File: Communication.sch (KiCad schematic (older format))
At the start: 8 parts

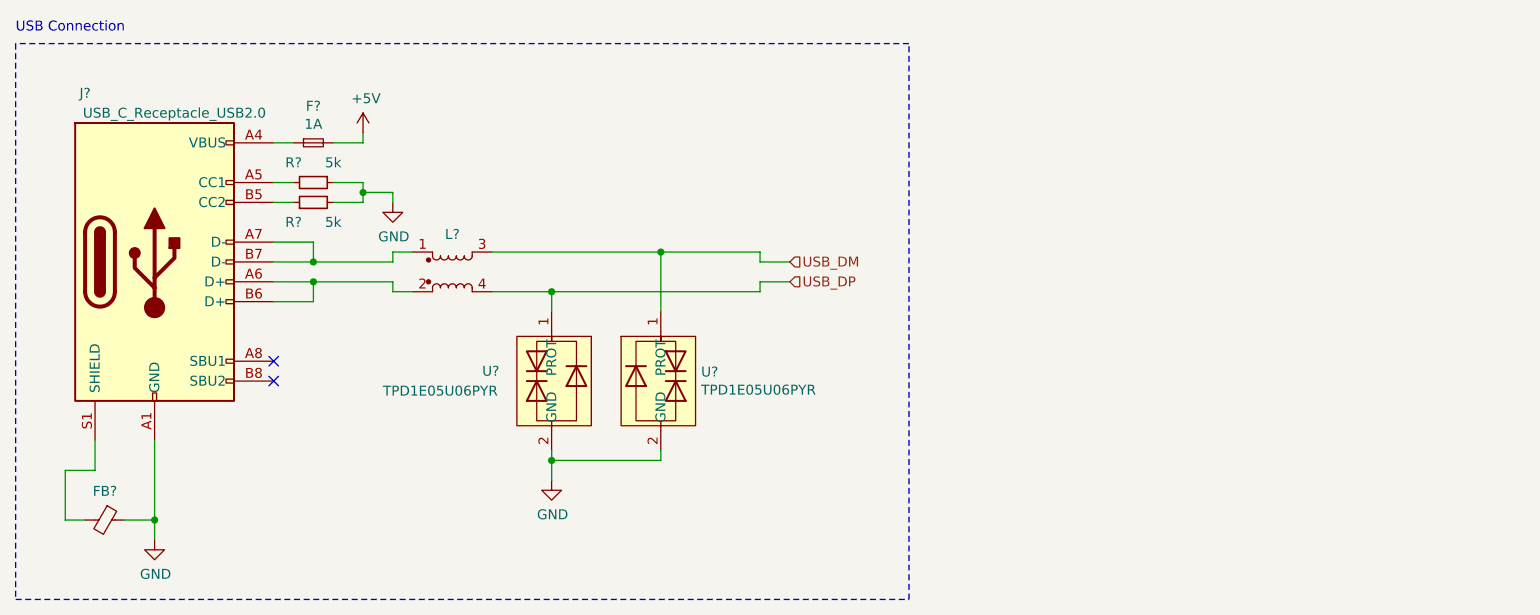
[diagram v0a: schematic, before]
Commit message: Added display driver for 7 segment
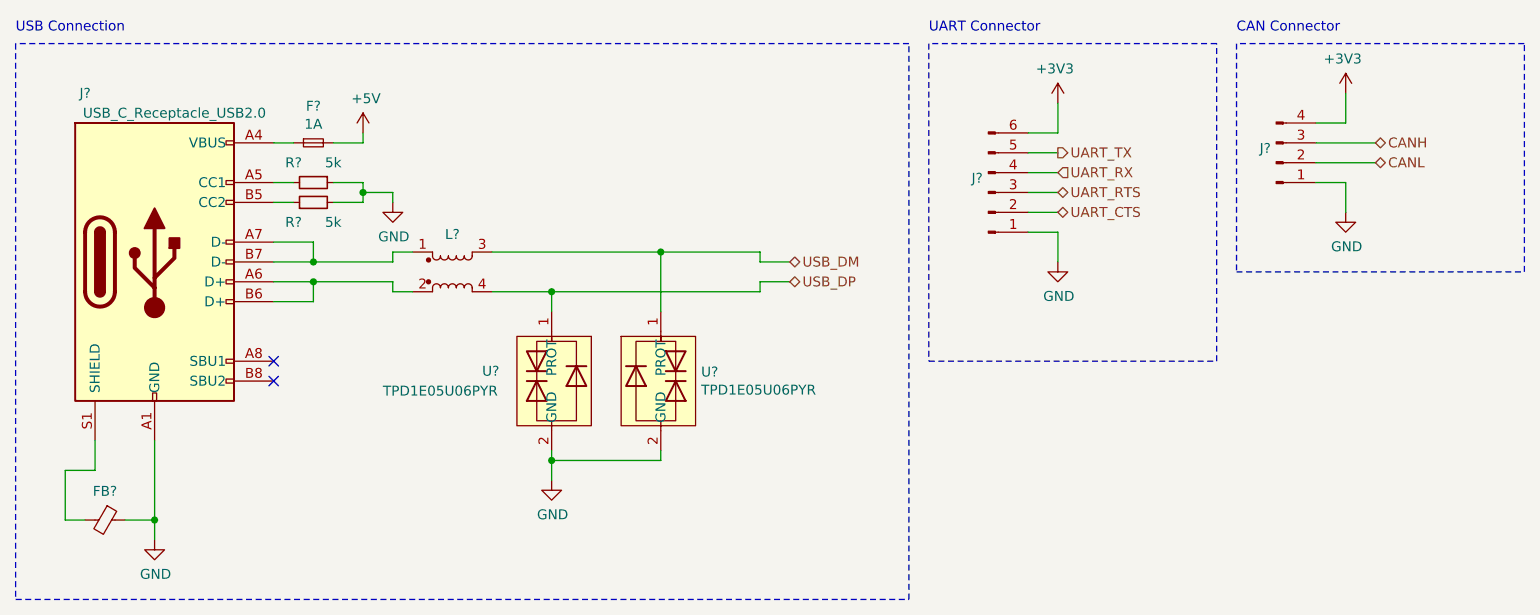
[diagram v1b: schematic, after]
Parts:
- added J?: Conn_01x06_Male, symbol Connector:Conn_01x06_Male
- added J?: Conn_01x04_Male, symbol Connector:Conn_01x04_Male
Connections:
- net GND: now also J?.1 (Pin_1), J?.1 (Pin_1)
- new net +3V3: J?.4 (Pin_4), J?.6 (Pin_6)
- new net CANH: J?.3 (Pin_3)
- new net CANL: J?.2 (Pin_2)
- new net UART_CTS: J?.2 (Pin_2)
- new net UART_RTS: J?.3 (Pin_3)
- new net UART_RX: J?.4 (Pin_4)
- new net UART_TX: J?.5 (Pin_5)
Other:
- note added: "CAN Connector"
- note added: "UART Connector"
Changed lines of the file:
@@
 $Descr A4 11693 8268
 encoding utf-8
-Sheet 1 7
+Sheet 5 7
 Title ""
 Date ""
@@
 Wire Wire Line
 	1850 1850 2050 1850
-Text HLabel 4450 1850 2    50   Input ~ 0
+Text HLabel 4450 1850 2    50   BiDi ~ 0
 USB_DP
 Wire Wire Line
@@
 	1    0    0    -1
 $EndComp
-Text HLabel 4450 1750 2    50   Input ~ 0
+Text HLabel 4450 1750 2    50   BiDi ~ 0
 USB_DM
 NoConn ~ 1850 2350
@@
 Text Notes 550  600  0    50   ~ 0
 USB Connection
+Text HLabel 5800 1200 2    50   Output ~ 0
+UART_TX
+Text HLabel 5800 1300 2    50   Input ~ 0
+UART_RX
+Text HLabel 5800 1400 2    50   BiDi ~ 0
+UART_RTS
+Text HLabel 5800 1500 2    50   BiDi ~ 0
+UART_CTS
+$Comp
+L Connector:Conn_01x06_Male J?
+U 1 1 5F695AB7
+P 5450 1400
+F 0 "J?" H 5422 1328 50  0000 R CNN
+F 1 "Conn_01x06_Male" H 5422 1373 50  0001 R CNN
+F 2 "" H 5450 1400 50  0001 C CNN
+F 3 "~" H 5450 1400 50  0001 C CNN
+	1    5450 1400
+	1    0    0    1
+$EndComp
+Wire Wire Line
+	5800 1200 5650 1200
+Wire Wire Line
+	5800 1300 5650 1300
+Wire Wire Line
+	5800 1400 5650 1400
+Wire Wire Line
+	5800 1500 5650 1500
+$Comp
+L power:GND #PWR?
+U 1 1 5F699450
+P 7250 1500
+F 0 "#PWR?" H 7250 1250 50  0001 C CNN
+F 1 "GND" H 7255 1327 50  0000 C CNN
+F 2 "" H 7250 1500 50  0001 C CNN
+F 3 "" H 7250 1500 50  0001 C CNN
+	1    7250 1500
+	1    0    0    -1
+$EndComp
+Wire Wire Line
+	5800 1600 5650 1600
+Wire Wire Line
+	5800 1600 5800 1750
+Wire Wire Line
+	5650 1100 5800 1100
+Wire Wire Line
+	5800 1100 5800 950
+$Comp
+L power:+3V3 #PWR?
+U 1 1 5F69C601
+P 5800 950
+F 0 "#PWR?" H 5800 800 50  0001 C CNN
+F 1 "+3V3" H 5815 1123 50  0000 C CNN
+F 2 "" H 5800 950 50  0001 C CNN
+F 3 "" H 5800 950 50  0001 C CNN
+	1    5800 950
+	-1   0    0    -1
+$EndComp
+Wire Notes Line
+	5150 650  5150 2250
+Wire Notes Line
+	5150 2250 6600 2250
+Wire Notes Line
+	6600 2250 6600 650
+Wire Notes Line
+	6600 650  5150 650
+Text Notes 5150 600  0    50   ~ 0
+UART Connector
+$Comp
+L Connector:Conn_01x04_Male J?
+U 1 1 5F6AA35C
+P 6900 1250
+F 0 "J?" H 6873 1178 50  0000 R CNN
+F 1 "Conn_01x04_Male" H 6872 1223 50  0001 R CNN
+F 2 "" H 6900 1250 50  0001 C CNN
+F 3 "~" H 6900 1250 50  0001 C CNN
+	1    6900 1250
+	1    0    0    1
+$EndComp
+$Comp
+L power:GND #PWR?
+U 1 1 5F6AD280
+P 5800 1750
+F 0 "#PWR?" H 5800 1500 50  0001 C CNN
+F 1 "GND" H 5805 1577 50  0000 C CNN
+F 2 "" H 5800 1750 50  0001 C CNN
+F 3 "" H 5800 1750 50  0001 C CNN
+	1    5800 1750
+	1    0    0    -1
+$EndComp
+Wire Wire Line
+	7250 1500 7250 1350
+Wire Wire Line
+	7250 1350 7100 1350
+Wire Wire Line
+	7100 1050 7250 1050
+Wire Wire Line
+	7250 1050 7250 900
+$Comp
+L power:+3V3 #PWR?
+U 1 1 5F6AF4CD
+P 7250 900
+F 0 "#PWR?" H 7250 750 50  0001 C CNN
+F 1 "+3V3" H 7265 1073 50  0000 C CNN
+F 2 "" H 7250 900 50  0001 C CNN
+F 3 "" H 7250 900 50  0001 C CNN
+	1    7250 900
+	-1   0    0    -1
+$EndComp
+Wire Wire Line
+	7100 1150 7400 1150
+Wire Wire Line
+	7100 1250 7400 1250
+Text HLabel 7400 1150 2    50   BiDi ~ 0
+CANH
+Text HLabel 7400 1250 2    50   BiDi ~ 0
+CANL
+Wire Notes Line
+	6700 650  6700 1800
+Wire Notes Line
+	6700 1800 8150 1800
+Wire Notes Line
+	8150 1800 8150 650
+Wire Notes Line
+	8150 650  6700 650
+Text Notes 6700 600  0    50   ~ 0
+CAN Connector
 $EndSCHEMATC

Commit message: Done with preliminary schematic. Needs review
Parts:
- R701, R702: renamed from R?; footprint (none) -> Resistor_SMD:R_0603_1608Metric
- gave numbers to parts that had none: 8
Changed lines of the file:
@@
 $Descr A4 11693 8268
 encoding utf-8
-Sheet 5 7
+Sheet 7 7
 Title ""
 Date ""
@@
 	1850 1650 2050 1650
 $Comp
-L Connector:USB_C_Receptacle_USB2.0 J?
+L Connector:USB_C_Receptacle_USB2.0 J703
 U 1 1 5F6A4CDA
 P 1250 1750
-F 0 "J?" H 900 2600 50  0000 C CNN
+F 0 "J703" H 900 2600 50  0000 C CNN
 F 1 "USB_C_Receptacle_USB2.0" H 1350 2500 50  0000 C CNN
 F 2 "" H 1400 1750 50  0001 C CNN
@@
 	1850 1150 1950 1150
 $Comp
-L Device:Fuse_Small F?
+L Device:Fuse_Small F701
 U 1 1 5F68858B
 P 2050 1150
-F 0 "F?" H 2050 1335 50  0000 C CNN
+F 0 "F701" H 2050 1335 50  0000 C CNN
 F 1 "1A" H 2050 1244 50  0000 C CNN
 F 2 "" H 2050 1150 50  0001 C CNN
@@
 $EndComp
 $Comp
-L power:+5V #PWR?
+L power:+5V #PWR0703
 U 1 1 5F687B2C
 P 2300 1100
-F 0 "#PWR?" H 2300 950 50  0001 C CNN
+F 0 "#PWR0703" H 2300 950 50  0001 C CNN
 F 1 "+5V" H 2315 1273 50  0000 C CNN
 F 2 "" H 2300 1100 50  0001 C CNN
@@
 	1850 1450 1950 1450
 $Comp
-L Device:R_Small R?
+L Device:R_Small R701
 U 1 1 5F6AD52B
 P 2050 1350
-F 0 "R?" V 1950 1250 50  0000 C CNN
+F 0 "R701" V 1950 1250 50  0000 C CNN
 F 1 "5k" V 1950 1450 50  0000 C CNN
-F 2 "" H 2050 1350 50  0001 C CNN
+F 2 "Resistor_SMD:R_0603_1608Metric" H 2050 1350 50  0001 C CNN
 F 3 "~" H 2050 1350 50  0001 C CNN
 	1    2050 1350
@@
 $EndComp
 $Comp
-L Device:R_Small R?
+L Device:R_Small R702
 U 1 1 5F6AE3C1
 P 2050 1450
-F 0 "R?" V 1950 1550 50  0000 C CNN
+F 0 "R702" V 1950 1550 50  0000 C CNN
 F 1 "5k" V 1950 1350 50  0000 C CNN
-F 2 "" H 2050 1450 50  0001 C CNN
+F 2 "Resistor_SMD:R_0603_1608Metric" H 2050 1450 50  0001 C CNN
 F 3 "~" H 2050 1450 50  0001 C CNN
 	1    2050 1450
@@
 	2300 1400 2300 1450
 $Comp
-L power:GND #PWR?
+L power:GND #PWR0704
 U 1 1 5F6AECB5
 P 2450 1450
-F 0 "#PWR?" H 2450 1200 50  0001 C CNN
+F 0 "#PWR0704" H 2450 1200 50  0001 C CNN
 F 1 "GND" H 2455 1277 50  0000 C CNN
 F 2 "" H 2450 1450 50  0001 C CNN
@@
 NoConn ~ 1850 2250
 $Comp
-L Device:FerriteBead_Small FB?
+L Device:FerriteBead_Small FB701
 U 1 1 5F6B6430
 P 1000 3050
-F 0 "FB?" V 855 3050 50  0000 C CNN
+F 0 "FB701" V 855 3050 50  0000 C CNN
 F 1 "FerriteBead_Small" V 854 3050 50  0001 C CNN
 F 2 "" V 930 3050 50  0001 C CNN
@@
 	1100 3050 1250 3050
 $Comp
-L power:GND #PWR?
+L power:GND #PWR0708
 U 1 1 5F687584
 P 1250 3150
-F 0 "#PWR?" H 1250 2900 50  0001 C CNN
+F 0 "#PWR0708" H 1250 2900 50  0001 C CNN
 F 1 "GND" H 1255 2977 50  0000 C CNN
 F 2 "" H 1250 3150 50  0001 C CNN
@@
 	1250 3050 1250 3150
 $Comp
-L Device:L_Coupled_Small_1324 L?
+L Device:L_Coupled_Small_1324 L701
 U 1 1 5F6BB274
 P 2750 1800
-F 0 "L?" H 2750 1989 50  0000 C CNN
+F 0 "L701" H 2750 1989 50  0000 C CNN
 F 1 "L_Coupled_Small_1324" H 2750 1990 50  0001 C CNN
 F 2 "" H 2750 1800 50  0001 C CNN
@@
 Connection ~ 2050 1850
 $Comp
-L ReflowOven:TPD1E05U06PYR U?
+L ReflowOven:TPD1E05U06PYR U701
 U 1 1 5F6D42E0
 P 3300 2350
-F 0 "U?" H 3700 2400 50  0000 R CNN
+F 0 "U701" H 3750 2400 50  0000 R CNN
 F 1 "TPD1E05U06PYR" H 4200 2300 50  0000 R CNN
 F 2 "" H 3425 2425 50  0001 C CNN
@@
 $EndComp
 $Comp
-L ReflowOven:TPD1E05U06PYR U?
+L ReflowOven:TPD1E05U06PYR U702
 U 1 1 5F6D65F6
 P 3750 2350
-F 0 "U?" H 4003 2396 50  0000 L CNN
+F 0 "U702" H 4003 2396 50  0000 L CNN
 F 1 "TPD1E05U06PYR" H 4003 2305 50  0000 L CNN
 F 2 "" H 3875 2425 50  0001 C CNN
@@
 	3800 2750 3800 2700
 $Comp
-L power:GND #PWR?
+L power:GND #PWR0707
 U 1 1 5F6D919F
 P 3250 2850
-F 0 "#PWR?" H 3250 2600 50  0001 C CNN
+F 0 "#PWR0707" H 3250 2600 50  0001 C CNN
 F 1 "GND" H 3255 2677 50  0000 C CNN
 F 2 "" H 3250 2850 50  0001 C CNN
@@
 UART_CTS
 $Comp
-L Connector:Conn_01x06_Male J?
+L Connector:Conn_01x06_Male J702
 U 1 1 5F695AB7
 P 5450 1400
-F 0 "J?" H 5422 1328 50  0000 R CNN
+F 0 "J702" H 5422 1328 50  0000 R CNN
 F 1 "Conn_01x06_Male" H 5422 1373 50  0001 R CNN
 F 2 "" H 5450 1400 50  0001 C CNN
@@
 	5800 1500 5650 1500
 $Comp
-L power:GND #PWR?
+L power:GND #PWR0705
 U 1 1 5F699450
 P 7250 1500
-F 0 "#PWR?" H 7250 1250 50  0001 C CNN
+F 0 "#PWR0705" H 7250 1250 50  0001 C CNN
 F 1 "GND" H 7255 1327 50  0000 C CNN
 F 2 "" H 7250 1500 50  0001 C CNN
@@
 	5800 1100 5800 950
 $Comp
-L power:+3V3 #PWR?
+L power:+3V3 #PWR0702
 U 1 1 5F69C601
 P 5800 950
-F 0 "#PWR?" H 5800 800 50  0001 C CNN
+F 0 "#PWR0702" H 5800 800 50  0001 C CNN
 F 1 "+3V3" H 5815 1123 50  0000 C CNN
 F 2 "" H 5800 950 50  0001 C CNN
@@
 UART Connector
 $Comp
-L Connector:Conn_01x04_Male J?
+L Connector:Conn_01x04_Male J701
 U 1 1 5F6AA35C
 P 6900 1250
-F 0 "J?" H 6873 1178 50  0000 R CNN
+F 0 "J701" H 6873 1178 50  0000 R CNN
 F 1 "Conn_01x04_Male" H 6872 1223 50  0001 R CNN
 F 2 "" H 6900 1250 50  0001 C CNN
@@
 $EndComp
 $Comp
-L power:GND #PWR?
+L power:GND #PWR0706
 U 1 1 5F6AD280
 P 5800 1750
-F 0 "#PWR?" H 5800 1500 50  0001 C CNN
+F 0 "#PWR0706" H 5800 1500 50  0001 C CNN
 F 1 "GND" H 5805 1577 50  0000 C CNN
 F 2 "" H 5800 1750 50  0001 C CNN
@@
 	7250 1050 7250 900
 $Comp
-L power:+3V3 #PWR?
+L power:+3V3 #PWR0701
 U 1 1 5F6AF4CD
 P 7250 900
-F 0 "#PWR?" H 7250 750 50  0001 C CNN
+F 0 "#PWR0701" H 7250 750 50  0001 C CNN
 F 1 "+3V3" H 7265 1073 50  0000 C CNN
 F 2 "" H 7250 900 50  0001 C CNN

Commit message: Added stuff
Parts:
- added J701: Conn_01x03_Male, Connector_PinHeader_1.00mm:PinHeader_1x03_P1.00mm_Vertical, symbol Connector:Conn_01x03_Male
- FB701: footprint (none) -> Inductor_SMD:L_0603_1608Metric
- J702: renamed from J701; value Conn_01x04_Male -> Microfit-4pin
- J703: renamed from J702; footprint (none) -> Connector_PinHeader_1.00mm:PinHeader_1x06_P1.00mm_Vertical
- U701, U702: footprint (none) -> Diode_SMD:D_0402_1005Metric
- renumbered J703 to J704
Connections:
- net +3V3: now also J701.1 (Pin_1); no longer J703.6 (Pin_6)
- new net: J701.2 (Pin_2), J703.6 (Pin_6)
- no-connect marks 2 -> 3
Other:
- moved on the sheet: J702
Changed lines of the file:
@@
 	1850 1650 2050 1650
 $Comp
-L Connector:USB_C_Receptacle_USB2.0 J703
+L Connector:USB_C_Receptacle_USB2.0 J704
 U 1 1 5F6A4CDA
 P 1250 1750
-F 0 "J703" H 900 2600 50  0000 C CNN
+F 0 "J704" H 900 2600 50  0000 C CNN
 F 1 "USB_C_Receptacle_USB2.0" H 1350 2500 50  0000 C CNN
 F 2 "" H 1400 1750 50  0001 C CNN
@@
 F 0 "FB701" V 855 3050 50  0000 C CNN
 F 1 "FerriteBead_Small" V 854 3050 50  0001 C CNN
-F 2 "" V 930 3050 50  0001 C CNN
+F 2 "Inductor_SMD:L_0603_1608Metric" V 930 3050 50  0001 C CNN
 F 3 "~" H 1000 3050 50  0001 C CNN
 	1    1000 3050
@@
 F 0 "U701" H 3750 2400 50  0000 R CNN
 F 1 "TPD1E05U06PYR" H 4200 2300 50  0000 R CNN
-F 2 "" H 3425 2425 50  0001 C CNN
+F 2 "Diode_SMD:D_0402_1005Metric" H 3425 2425 50  0001 C CNN
 F 3 "" H 3425 2425 50  0001 C CNN
 	1    3300 2350
@@
 F 0 "U702" H 4003 2396 50  0000 L CNN
 F 1 "TPD1E05U06PYR" H 4003 2305 50  0000 L CNN
-F 2 "" H 3875 2425 50  0001 C CNN
+F 2 "Diode_SMD:D_0402_1005Metric" H 3875 2425 50  0001 C CNN
 F 3 "" H 3875 2425 50  0001 C CNN
 	1    3750 2350
@@
 UART_CTS
 $Comp
-L Connector:Conn_01x06_Male J702
+L Connector:Conn_01x06_Male J703
 U 1 1 5F695AB7
 P 5450 1400
-F 0 "J702" H 5422 1328 50  0000 R CNN
+F 0 "J703" H 5422 1328 50  0000 R CNN
 F 1 "Conn_01x06_Male" H 5422 1373 50  0001 R CNN
-F 2 "" H 5450 1400 50  0001 C CNN
+F 2 "Connector_PinHeader_1.00mm:PinHeader_1x06_P1.00mm_Vertical" H 5450 1400 50  0001 C CNN
 F 3 "~" H 5450 1400 50  0001 C CNN
 	1    5450 1400
@@
 L power:GND #PWR0705
 U 1 1 5F699450
-P 7250 1500
-F 0 "#PWR0705" H 7250 1250 50  0001 C CNN
-F 1 "GND" H 7255 1327 50  0000 C CNN
-F 2 "" H 7250 1500 50  0001 C CNN
-F 3 "" H 7250 1500 50  0001 C CNN
-	1    7250 1500
+P 7450 1500
+F 0 "#PWR0705" H 7450 1250 50  0001 C CNN
+F 1 "GND" H 7455 1327 50  0000 C CNN
+F 2 "" H 7450 1500 50  0001 C CNN
+F 3 "" H 7450 1500 50  0001 C CNN
+	1    7450 1500
 	1    0    0    -1
 $EndComp
@@
 	5800 1600 5800 1750
 Wire Wire Line
-	5650 1100 5800 1100
-Wire Wire Line
-	5800 1100 5800 950
-$Comp
-L power:+3V3 #PWR0702
+	6400 1100 6400 900
+$Comp
+L power:+3V3 #PWR0701
 U 1 1 5F69C601
-P 5800 950
-F 0 "#PWR0702" H 5800 800 50  0001 C CNN
-F 1 "+3V3" H 5815 1123 50  0000 C CNN
-F 2 "" H 5800 950 50  0001 C CNN
-F 3 "" H 5800 950 50  0001 C CNN
-	1    5800 950
+P 6400 900
+F 0 "#PWR0701" H 6400 750 50  0001 C CNN
+F 1 "+3V3" H 6415 1073 50  0000 C CNN
+F 2 "" H 6400 900 50  0001 C CNN
+F 3 "" H 6400 900 50  0001 C CNN
+	1    6400 900
 	-1   0    0    -1
 $EndComp
@@
 UART Connector
 $Comp
-L Connector:Conn_01x04_Male J701
+L Connector:Conn_01x04_Male J702
 U 1 1 5F6AA35C
-P 6900 1250
-F 0 "J701" H 6873 1178 50  0000 R CNN
-F 1 "Conn_01x04_Male" H 6872 1223 50  0001 R CNN
-F 2 "" H 6900 1250 50  0001 C CNN
-F 3 "~" H 6900 1250 50  0001 C CNN
-	1    6900 1250
+P 7100 1250
+F 0 "J702" H 7073 1178 50  0000 R CNN
+F 1 "Microfit-4pin" H 7072 1223 50  0001 R CNN
+F 2 "" H 7100 1250 50  0001 C CNN
+F 3 "~" H 7100 1250 50  0001 C CNN
+	1    7100 1250
 	1    0    0    1
 $EndComp
@@
 $EndComp
 Wire Wire Line
-	7250 1500 7250 1350
-Wire Wire Line
-	7250 1350 7100 1350
-Wire Wire Line
-	7100 1050 7250 1050
-Wire Wire Line
-	7250 1050 7250 900
-$Comp
-L power:+3V3 #PWR0701
+	7450 1500 7450 1350
+Wire Wire Line
+	7450 1350 7300 1350
+Wire Wire Line
+	7300 1050 7450 1050
+Wire Wire Line
+	7450 1050 7450 900
+$Comp
+L power:+3V3 #PWR0702
 U 1 1 5F6AF4CD
-P 7250 900
-F 0 "#PWR0701" H 7250 750 50  0001 C CNN
-F 1 "+3V3" H 7265 1073 50  0000 C CNN
-F 2 "" H 7250 900 50  0001 C CNN
-F 3 "" H 7250 900 50  0001 C CNN
-	1    7250 900
+P 7450 900
+F 0 "#PWR0702" H 7450 750 50  0001 C CNN
+F 1 "+3V3" H 7465 1073 50  0000 C CNN
+F 2 "" H 7450 900 50  0001 C CNN
+F 3 "" H 7450 900 50  0001 C CNN
+	1    7450 900
 	-1   0    0    -1
 $EndComp
 Wire Wire Line
-	7100 1150 7400 1150
-Wire Wire Line
-	7100 1250 7400 1250
-Text HLabel 7400 1150 2    50   BiDi ~ 0
+	7300 1150 7600 1150
+Wire Wire Line
+	7300 1250 7600 1250
+Text HLabel 7600 1150 2    50   BiDi ~ 0
 CANH
-Text HLabel 7400 1250 2    50   BiDi ~ 0
+Text HLabel 7600 1250 2    50   BiDi ~ 0
 CANL
 Wire Notes Line
@@
 Text Notes 6700 600  0    50   ~ 0
 CAN Connector
+$Comp
+L Connector:Conn_01x03_Male J701
+U 1 1 5F71B578
+P 5900 750
+F 0 "J701" V 5962 894 50  0000 L CNN
+F 1 "Conn_01x03_Male" V 5850 400 50  0000 L CNN
+F 2 "Connector_PinHeader_1.00mm:PinHeader_1x03_P1.00mm_Vertical" H 5900 750 50  0001 C CNN
+F 3 "~" H 5900 750 50  0001 C CNN
+	1    5900 750
+	0    1    1    0
+$EndComp
+Wire Wire Line
+	6000 1100 6000 950
+Wire Wire Line
+	6000 1100 6400 1100
+Wire Wire Line
+	5900 950  5900 1100
+Wire Wire Line
+	5900 1100 5650 1100
+NoConn ~ 5800 950
 $EndSCHEMATC

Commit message: Added some footprints
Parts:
- L701: footprint (none) -> ReflowOven:744231091
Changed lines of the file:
@@
 F 0 "L701" H 2750 1989 50  0000 C CNN
 F 1 "L_Coupled_Small_1324" H 2750 1990 50  0001 C CNN
-F 2 "" H 2750 1800 50  0001 C CNN
+F 2 "ReflowOven:744231091" H 2750 1800 50  0001 C CNN
 F 3 "~" H 2750 1800 50  0001 C CNN
 	1    2750 1800

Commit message: Done with footprints
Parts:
- F701: footprint (none) -> ReflowOven:FUSC6125X279N
- J702: footprint (none) -> Connector_PinHeader_1.00mm:PinHeader_2x02_P1.00mm_Vertical
- J704: footprint (none) -> Connector_USB:USB_C_Receptacle_Amphenol_12401610E4-2A
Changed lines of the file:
@@
 F 0 "J704" H 900 2600 50  0000 C CNN
 F 1 "USB_C_Receptacle_USB2.0" H 1350 2500 50  0000 C CNN
-F 2 "" H 1400 1750 50  0001 C CNN
+F 2 "Connector_USB:USB_C_Receptacle_Amphenol_12401610E4-2A" H 1400 1750 50  0001 C CNN
 F 3 "https://www.usb.org/sites/default/files/documents/usb_type-c.zip" H 1400 1750 50  0001 C CNN
 	1    1250 1750
@@
 F 0 "F701" H 2050 1335 50  0000 C CNN
 F 1 "1A" H 2050 1244 50  0000 C CNN
-F 2 "" H 2050 1150 50  0001 C CNN
+F 2 "ReflowOven:FUSC6125X279N" H 2050 1150 50  0001 C CNN
 F 3 "~" H 2050 1150 50  0001 C CNN
 	1    2050 1150
@@
 F 0 "J702" H 7073 1178 50  0000 R CNN
 F 1 "Microfit-4pin" H 7072 1223 50  0001 R CNN
-F 2 "" H 7100 1250 50  0001 C CNN
+F 2 "Connector_PinHeader_1.00mm:PinHeader_2x02_P1.00mm_Vertical" H 7100 1250 50  0001 C CNN
 F 3 "~" H 7100 1250 50  0001 C CNN
 	1    7100 1250

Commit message: Began routing
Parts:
- removed F701: 1A, ReflowOven:FUSC6125X279N, symbol Device:Fuse_Small
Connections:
- net USB_DM renamed USB_D-
- net USB_DP renamed USB_D+
- no-connect marks 3 -> 4
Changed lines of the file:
@@
 	1850 1850 2050 1850
 Text HLabel 4450 1850 2    50   BiDi ~ 0
-USB_DP
+USB_D+
 Wire Wire Line
 	1850 1650 2050 1650
@@
 	1    0    0    -1
 $EndComp
-Wire Wire Line
-	2150 1150 2300 1150
-Wire Wire Line
-	1850 1150 1950 1150
-$Comp
-L Device:Fuse_Small F701
-U 1 1 5F68858B
-P 2050 1150
-F 0 "F701" H 2050 1335 50  0000 C CNN
-F 1 "1A" H 2050 1244 50  0000 C CNN
-F 2 "ReflowOven:FUSC6125X279N" H 2050 1150 50  0001 C CNN
-F 3 "~" H 2050 1150 50  0001 C CNN
-	1    2050 1150
-	1    0    0    -1
-$EndComp
-$Comp
-L power:+5V #PWR0703
-U 1 1 5F687B2C
-P 2300 1100
-F 0 "#PWR0703" H 2300 950 50  0001 C CNN
-F 1 "+5V" H 2315 1273 50  0000 C CNN
-F 2 "" H 2300 1100 50  0001 C CNN
-F 3 "" H 2300 1100 50  0001 C CNN
-	1    2300 1100
-	1    0    0    -1
-$EndComp
-Wire Wire Line
-	2300 1150 2300 1100
 Wire Wire Line
 	2050 1650 2050 1750
@@
 $EndComp
 Text HLabel 4450 1750 2    50   BiDi ~ 0
-USB_DM
+USB_D-
 NoConn ~ 1850 2350
 NoConn ~ 1850 2250
@@
 	5900 1100 5650 1100
 NoConn ~ 5800 950
+NoConn ~ 1850 1150
 $EndSCHEMATC

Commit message: Done for today with layout
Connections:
- net CANH renamed CAN+
- net CANL renamed CAN-
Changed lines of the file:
@@
 	7300 1250 7600 1250
 Text HLabel 7600 1150 2    50   BiDi ~ 0
-CANH
+CAN+
 Text HLabel 7600 1250 2    50   BiDi ~ 0
-CANL
+CAN-
 Wire Notes Line
 	6700 650  6700 1800
